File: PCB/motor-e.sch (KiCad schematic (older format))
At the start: 28 parts

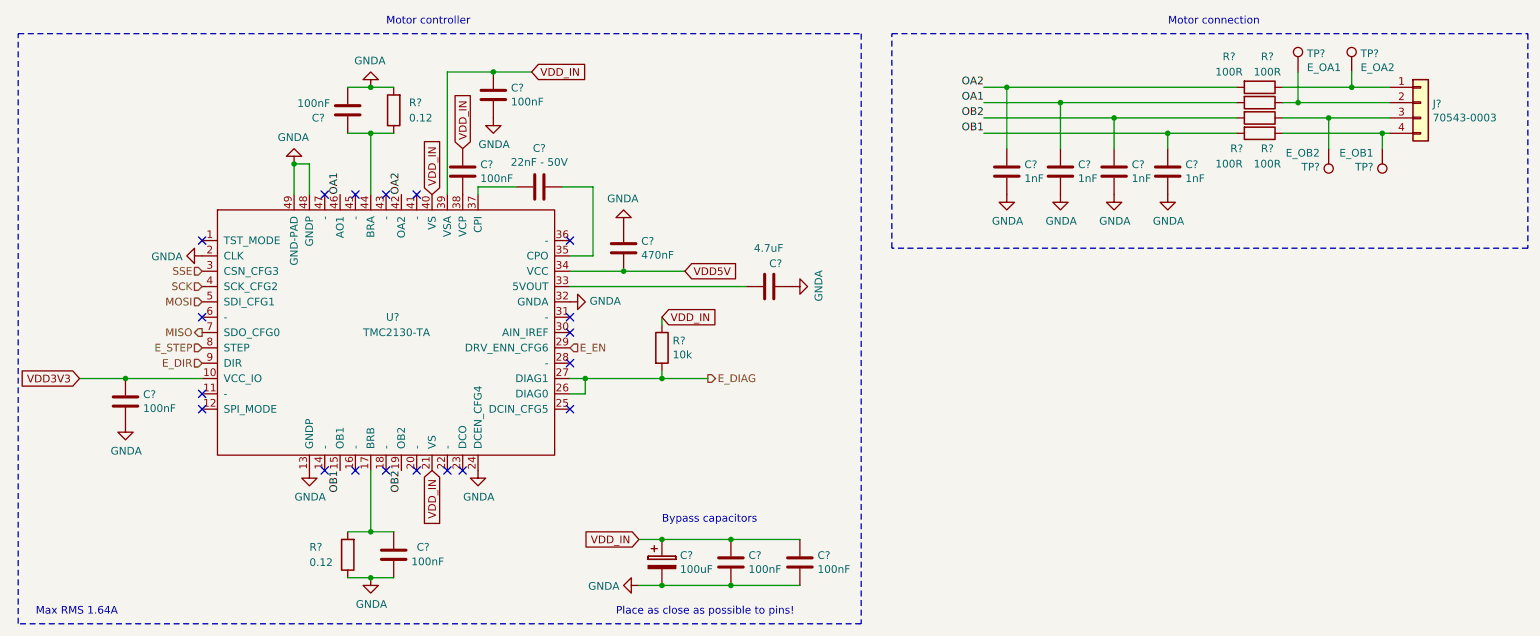
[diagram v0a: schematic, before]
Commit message: Fixed bugs found with ERC.
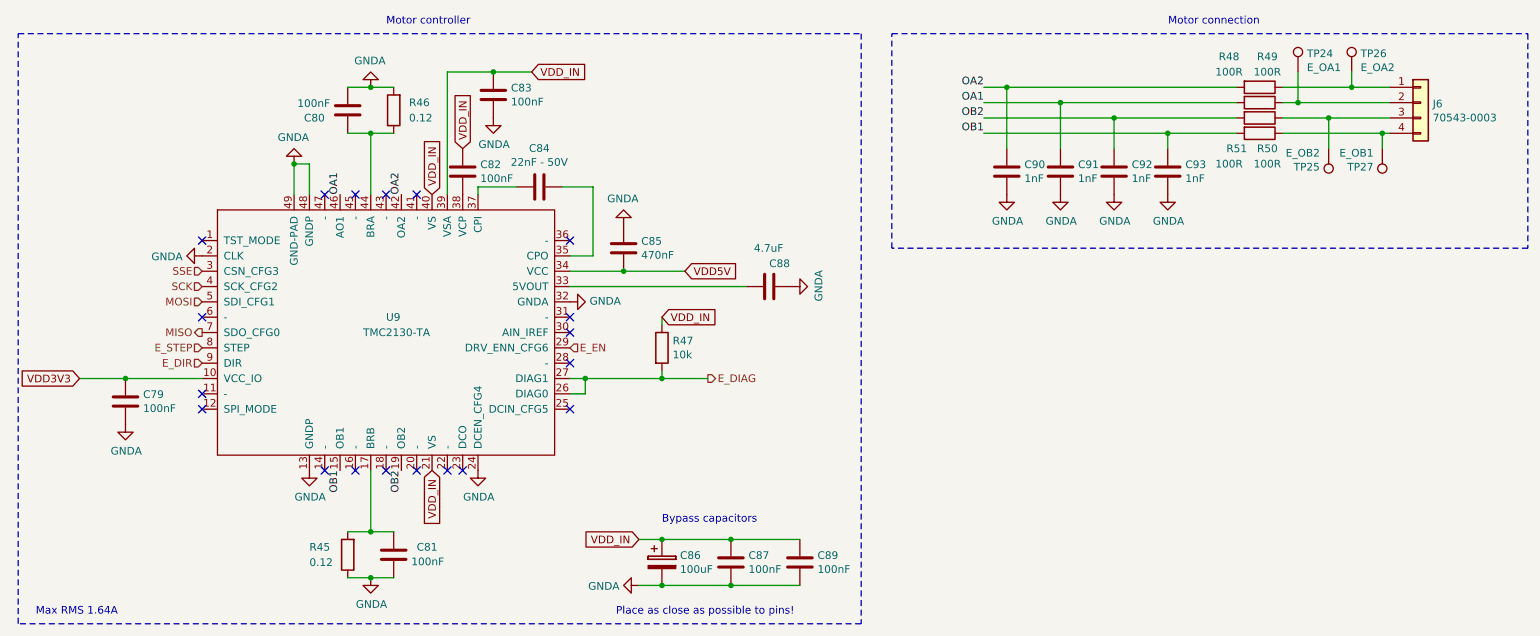
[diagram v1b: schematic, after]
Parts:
- removed C? (x4): 100nF, Capacitor_SMD:C_0603_1608Metric, symbol Device:C
- removed C?: 22nF - 50V, Capacitor_SMD:C_0603_1608Metric, symbol Device:C
- removed C?: 470nF, Capacitor_SMD:C_0603_1608Metric, symbol Device:C
- removed C? (x3): 1nF, Resistor_SMD:R_0603_1608Metric, symbol Device:C
- removed J?: 70543-0003, Connector_PinHeader_2.54mm:PinHeader_1x04_P2.54mm_Vertical, symbol Connector_Generic:Conn_01x04
- removed R?: 0.12, Resistor_SMD:R_1206_3216Metric, symbol Device:R
- removed R?: 10k, Resistor_SMD:R_0603_1608Metric, symbol Device:R
- removed R? (x4): 100R, Resistor_SMD:R_0603_1608Metric, symbol Device:R
- removed TP?: E_OA2, TestPoint:TestPoint_Pad_D1.0mm, symbol Connector_Specialized:Test_Point
- removed TP?: E_OA1, TestPoint:TestPoint_Pad_D1.0mm, symbol Connector_Specialized:Test_Point
- removed TP?: E_OB2, TestPoint:TestPoint_Pad_D1.0mm, symbol Connector_Specialized:Test_Point
- removed TP?: E_OB1, TestPoint:TestPoint_Pad_D1.0mm, symbol Connector_Specialized:Test_Point
- added C79, C80, C81, C82: 100nF, Capacitor_SMD:C_0603_1608Metric, symbol Device:C
- added C84: 22nF - 50V, Capacitor_SMD:C_0603_1608Metric, symbol Device:C
- added C85: 470nF, Capacitor_SMD:C_0603_1608Metric, symbol Device:C
- added C91, C92, C93: 1nF, Resistor_SMD:R_0603_1608Metric, symbol Device:C
- added J6: 70543-0003, Connector_PinHeader_2.54mm:PinHeader_1x04_P2.54mm_Vertical, symbol Connector_Generic:Conn_01x04
- added R46: 0.12, Resistor_SMD:R_1206_3216Metric, symbol Device:R
- added R47: 10k, Resistor_SMD:R_0603_1608Metric, symbol Device:R
- added R48, R49, R50, R51: 100R, Resistor_SMD:R_0603_1608Metric, symbol Device:R
- added TP24: E_OA1, TestPoint:TestPoint_Pad_D1.0mm, symbol Connector_Specialized:Test_Point
- added TP25: E_OB2, TestPoint:TestPoint_Pad_D1.0mm, symbol Connector_Specialized:Test_Point
- added TP26: E_OA2, TestPoint:TestPoint_Pad_D1.0mm, symbol Connector_Specialized:Test_Point
- added TP27: E_OB1, TestPoint:TestPoint_Pad_D1.0mm, symbol Connector_Specialized:Test_Point
- gave numbers to parts that had none: 8
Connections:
- net E_DIAG: now also R47.2
- net GNDA: now also C79.2, C80.2, C81.2, C85.2, C91.2, C92.2, C93.2, R46.2
- net OA1: now also C91.1, R49.2
- net OA2: now also R48.2
- net OB1: now also C93.1, R51.2
- net OB2: now also C92.1, R50.2
- net VDD3V3: now also C79.1
- net VDD5V: now also C85.1
- net VDD_IN: now also C82.1, R47.1
- net at U9.44 (BRA): now also C80.1, R46.1
- net at R45.2, U9.17 (BRB): now also C81.1
- net at U9.35 (CPO): now also C84.1
- net at U9.37 (CPI): now also C84.2
- net at U9.38 (VCP): now also C82.2
- new net: J6.1 (Pin_1), R48.1, TP26.1
- new net: J6.2 (Pin_2), R49.1, TP24.1
- new net: J6.3 (Pin_3), R50.1, TP25.1
- new net: J6.4 (Pin_4), R51.1, TP27.1

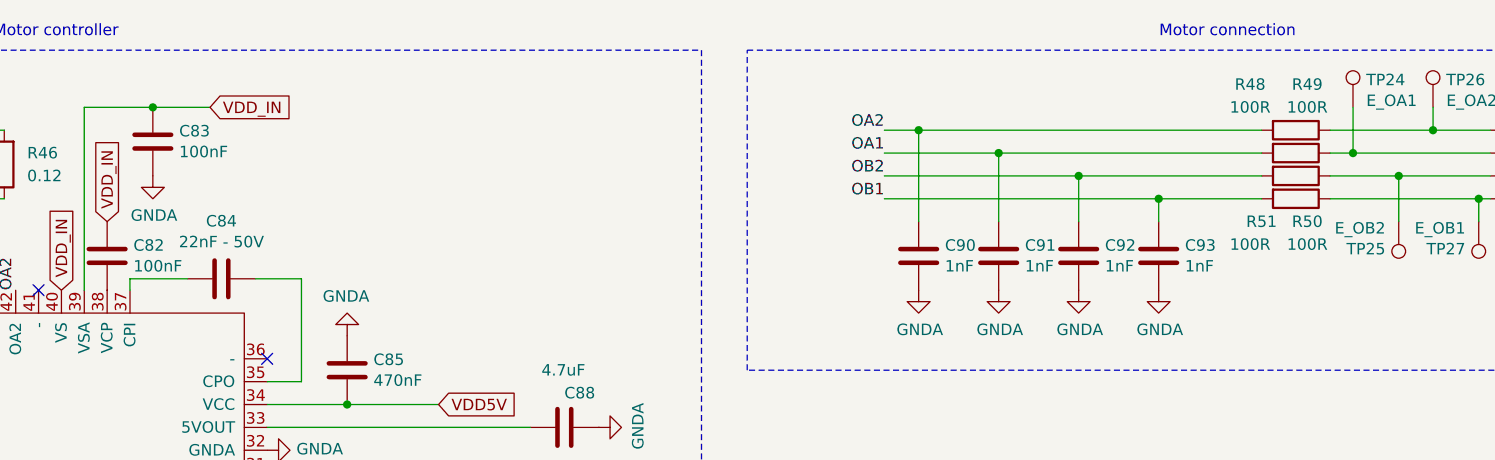
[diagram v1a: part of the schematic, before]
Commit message: Fixed annotations and assignment errors.
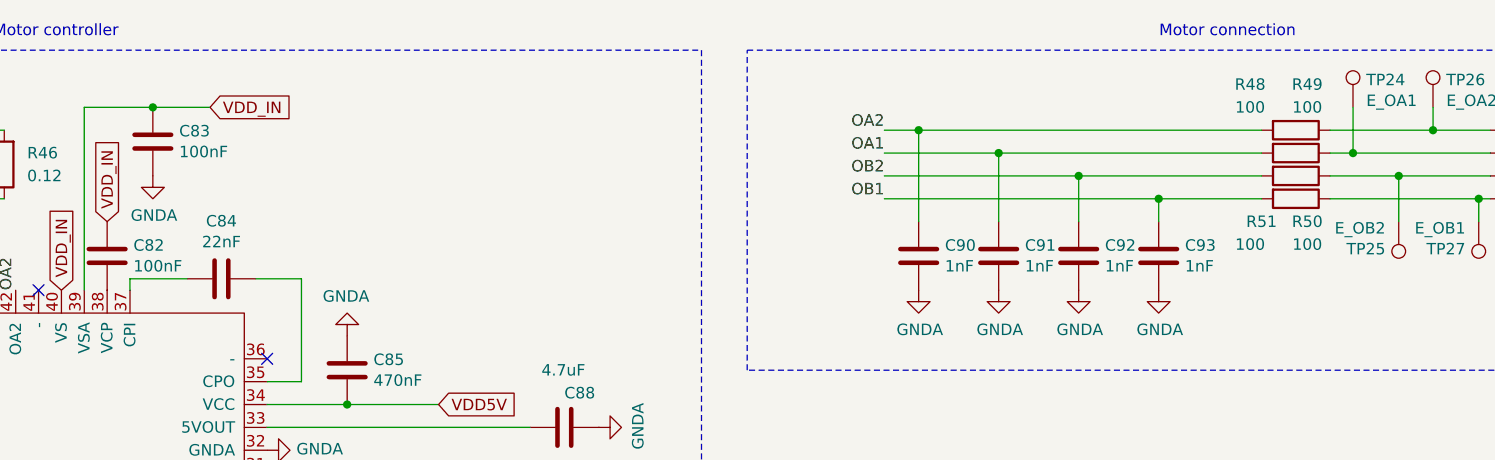
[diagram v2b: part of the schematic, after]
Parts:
- C84: value 22nF - 50V -> 22nF
- C88, C90, C91, C92, C93: footprint Resistor_SMD:R_0603_1608Metric -> Capacitor_SMD:C_0603_1608Metric
- R48, R49, R50, R51: value 100R -> 100
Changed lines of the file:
@@
 $Comp
 L remram-custom:TMC2130-TA U9
-U 1 1 5B0329FA
+U 1 1 5AF8CE99
 P 3000 2600
 F 0 "U9" H 2950 2650 50  0000 L CNN
@@
 $Comp
 L power:GNDA #PWR0106
-U 1 1 5B038691
+U 1 1 5AF8CE9B
 P 3550 3550
 F 0 "#PWR0106" H 3550 3300 50  0001 C CNN
@@
 P 3950 1700
 F 0 "C84" V 3698 1700 50  0000 C CNN
-F 1 "22nF - 50V" V 3789 1700 50  0000 C CNN
+F 1 "22nF" V 3789 1700 50  0000 C CNN
 F 2 "Capacitor_SMD:C_0603_1608Metric" H 3988 1550 50  0001 C CNN
 F 3 "~" H 3950 1700 50  0001 C CNN
@@
 $Comp
 L Device:C C83
-U 1 1 5B03C54C
+U 1 1 5AF8CEA4
 P 3650 1100
 F 0 "C83" H 3765 1146 50  0000 L CNN
@@
 $Comp
 L power:GNDA #PWR0107
-U 1 1 5B03CBB9
+U 1 1 5AF8CEA7
 P 3650 1250
 F 0 "#PWR0107" H 3650 1000 50  0001 C CNN
@@
 $Comp
 L Device:C C88
-U 1 1 5B044550
+U 1 1 5AF8CEAD
 P 5450 2350
 F 0 "C88" V 5600 2350 50  0000 R CNN
 F 1 "4.7uF" V 5700 2450 50  0000 R CNN
-F 2 "Resistor_SMD:R_0603_1608Metric" H 5488 2200 50  0001 C CNN
+F 2 "Capacitor_SMD:C_0603_1608Metric" H 5488 2200 50  0001 C CNN
 F 3 "~" H 5450 2350 50  0001 C CNN
 	1    5450 2350
@@
 P 8650 1350
 F 0 "R51" V 8750 1200 50  0000 C CNN
-F 1 "100R" V 8850 1150 50  0000 C CNN
+F 1 "100" V 8850 1150 50  0000 C CNN
 F 2 "Resistor_SMD:R_0603_1608Metric" V 8580 1350 50  0001 C CNN
 F 3 "~" H 8650 1350 50  0001 C CNN
@@
 F 0 "C93" H 8165 1646 50  0000 L CNN
 F 1 "1nF" H 8165 1555 50  0000 L CNN
-F 2 "Resistor_SMD:R_0603_1608Metric" H 8088 1450 50  0001 C CNN
+F 2 "Capacitor_SMD:C_0603_1608Metric" H 8088 1450 50  0001 C CNN
 F 3 "~" H 8050 1600 50  0001 C CNN
 	1    8050 1600
@@
 F 0 "C92" H 7815 1646 50  0000 L CNN
 F 1 "1nF" H 7815 1555 50  0000 L CNN
-F 2 "Resistor_SMD:R_0603_1608Metric" H 7738 1450 50  0001 C CNN
+F 2 "Capacitor_SMD:C_0603_1608Metric" H 7738 1450 50  0001 C CNN
 F 3 "~" H 7700 1600 50  0001 C CNN
 	1    7700 1600
@@
 F 0 "C91" H 7465 1646 50  0000 L CNN
 F 1 "1nF" H 7465 1555 50  0000 L CNN
-F 2 "Resistor_SMD:R_0603_1608Metric" H 7388 1450 50  0001 C CNN
+F 2 "Capacitor_SMD:C_0603_1608Metric" H 7388 1450 50  0001 C CNN
 F 3 "~" H 7350 1600 50  0001 C CNN
 	1    7350 1600
@@
 $Comp
 L Device:C C90
-U 1 1 5B0AD580
+U 1 1 5AF8CECE
 P 7000 1600
 F 0 "C90" H 7115 1646 50  0000 L CNN
 F 1 "1nF" H 7115 1555 50  0000 L CNN
-F 2 "Resistor_SMD:R_0603_1608Metric" H 7038 1450 50  0001 C CNN
+F 2 "Capacitor_SMD:C_0603_1608Metric" H 7038 1450 50  0001 C CNN
 F 3 "~" H 7000 1600 50  0001 C CNN
 	1    7000 1600
@@
 $Comp
 L power:GNDA #PWR0110
-U 1 1 5B0D4996
+U 1 1 5AF8CED4
 P 4600 4300
 F 0 "#PWR0110" H 4600 4050 50  0001 C CNN
@@
 $Comp
 L Device:CP C86
-U 1 1 5B0E8E43
+U 1 1 5AF8CED6
 P 4750 4150
 F 0 "C86" H 4868 4196 50  0000 L CNN
 F 1 "100uF" H 4868 4105 50  0000 L CNN
 F 2 "Capacitor_THT:CP_Radial_D6.3mm_P2.50mm" H 4788 4000 50  0001 C CNN
-F 3 "https://www.mouser.de/ProductDetail/Wurth-Electronics/860010573007?qs=sGAEpiMZZMvwFf0viD3Y3aZipiehufnXDo3pM9Qdgp1gvK74JBMa%252bg%3d%3d" H 4750 4150 50  0001 C CNN
+F 3 "https://eu.mouser.com/datasheet/2/293/e-uvz-1219460.pdf" H 4750 4150 50  0001 C CNN
 	1    4750 4150
 	1    0    0    -1
@@
 P 8650 1250
 F 0 "R50" V 8850 1300 50  0000 C CNN
-F 1 "100R" V 8950 1300 50  0000 C CNN
+F 1 "100" V 8950 1300 50  0000 C CNN
 F 2 "Resistor_SMD:R_0603_1608Metric" V 8580 1250 50  0001 C CNN
 F 3 "~" H 8650 1250 50  0001 C CNN
@@
 P 8650 1150
 F 0 "R49" V 8350 1200 50  0000 C CNN
-F 1 "100R" V 8450 1200 50  0000 C CNN
+F 1 "100" V 8450 1200 50  0000 C CNN
 F 2 "Resistor_SMD:R_0603_1608Metric" V 8580 1150 50  0001 C CNN
 F 3 "~" H 8650 1150 50  0001 C CNN
@@
 P 8650 1050
 F 0 "R48" V 8450 850 50  0000 C CNN
-F 1 "100R" V 8550 850 50  0000 C CNN
+F 1 "100" V 8550 850 50  0000 C CNN
 F 2 "Resistor_SMD:R_0603_1608Metric" V 8580 1050 50  0001 C CNN
 F 3 "~" H 8650 1050 50  0001 C CNN

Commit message: Saving work in progress.
Every component now has a 3D mode.
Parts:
- J6: footprint Connector_PinHeader_2.54mm:PinHeader_1x04_P2.54mm_Vertical -> custom-footprints:70543-0003
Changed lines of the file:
@@
 $Descr A4 11693 8268
 encoding utf-8
-Sheet 9 9
+Sheet 8 9
 Title "Motor Extruder"
 Date ""
@@
 F 0 "J6" H 9779 1142 50  0000 L CNN
 F 1 "70543-0003" H 9779 1051 50  0000 L CNN
-F 2 "Connector_PinHeader_2.54mm:PinHeader_1x04_P2.54mm_Vertical" H 9700 1150 50  0001 C CNN
+F 2 "custom-footprints:70543-0003" H 9700 1150 50  0001 C CNN
 F 3 "https://www.mouser.de/ProductDetail/Molex/70543-0003?qs=sGAEpiMZZMs%252bGHln7q6pm%252bS0pk2Wo0XxCD3CKlCQrmU%3d" H 9700 1150 50  0001 C CNN
 	1    9700 1150

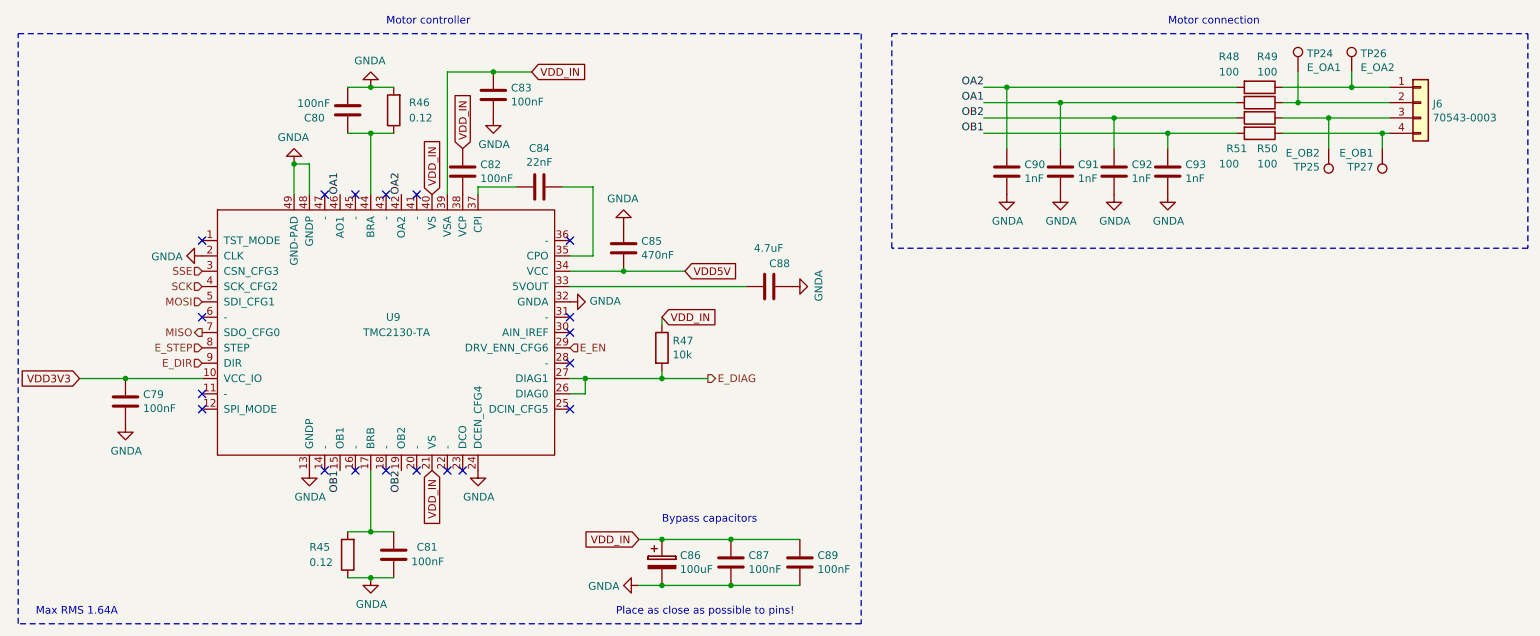
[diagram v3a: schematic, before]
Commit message: Removed logic level converter. Changed LDO.
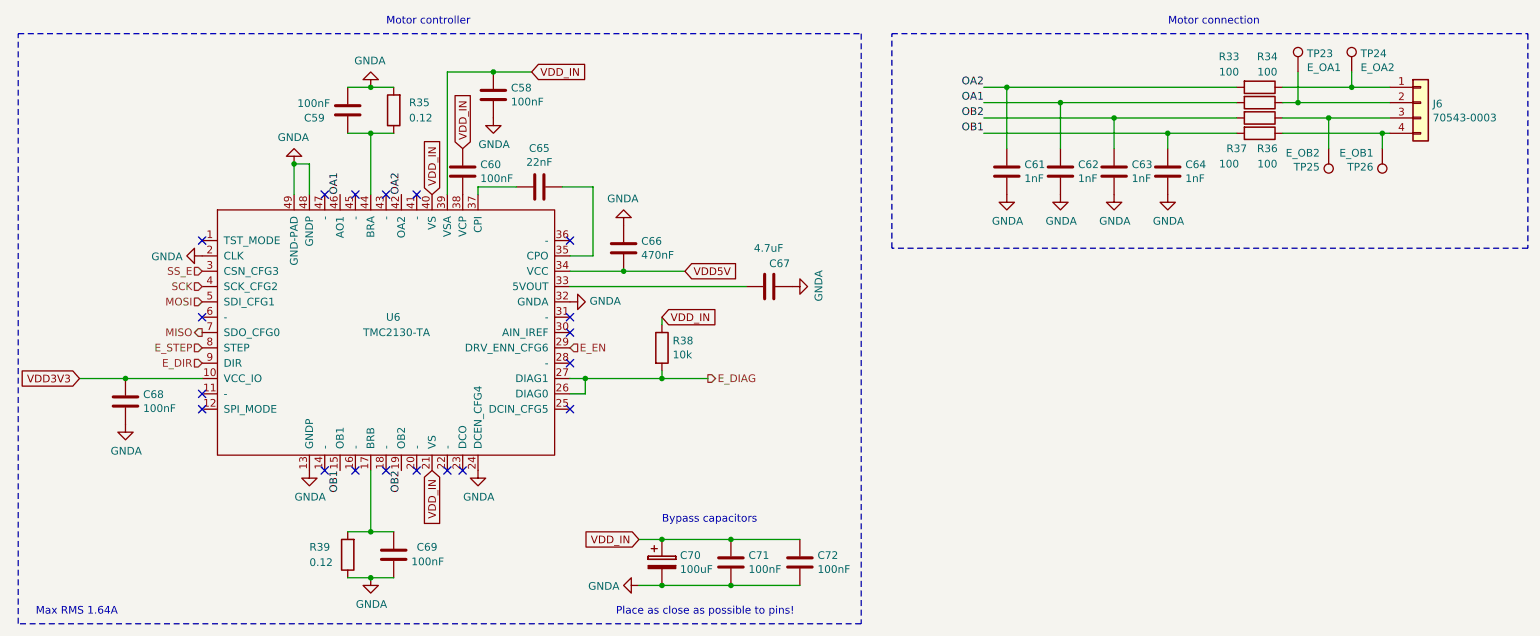
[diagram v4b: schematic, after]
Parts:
- renumbered C83 to C58, C80 to C59, C82 to C60, C90 to C61, C91 to C62, C92 to C63, C93 to C64, C84 to C65, C85 to C66, C88 to C67, C79 to C68, C81 to C69, C86 to C70, C87 to C71, C89 to C72, R48 to R33, R49 to R34, R46 to R35, R50 to R36, R51 to R37, R47 to R38, R45 to R39, TP24 to TP23, TP26 to TP24, TP27 to TP26, U9 to U6
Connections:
- net SSE renamed SS_E
